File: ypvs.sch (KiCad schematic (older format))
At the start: 17 parts, among them J1 Servo, J2 LM_2596 _Input, J3 HV_Cable, J4 Motorcycle Battery, U2 LM1117-3.3, U3 H11L1

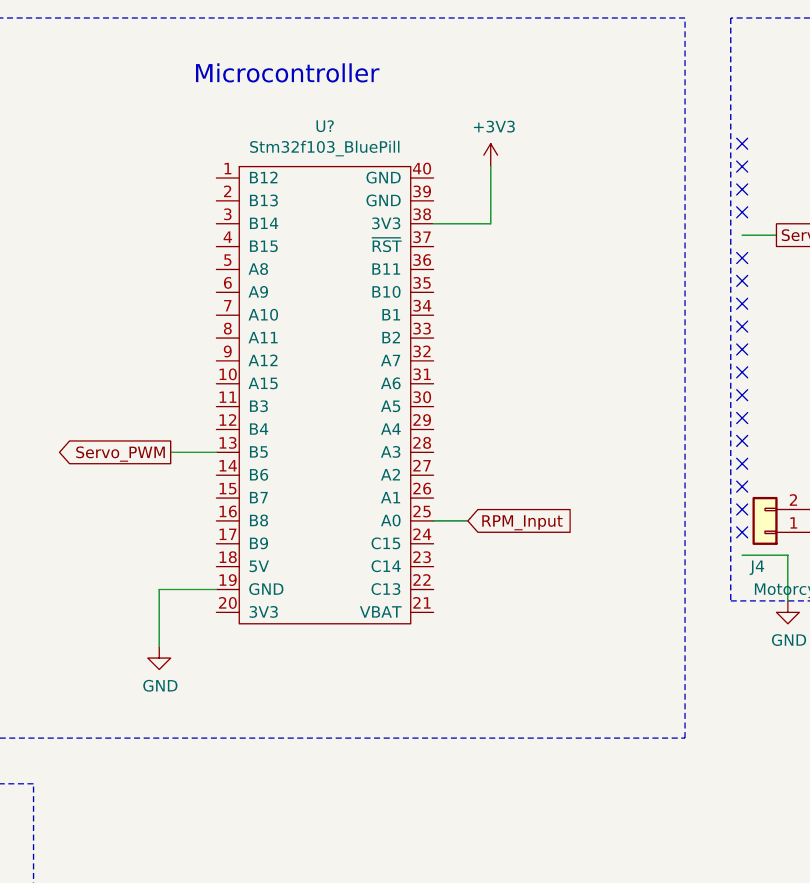
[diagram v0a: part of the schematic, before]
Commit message: added pcb outline and mounting holes
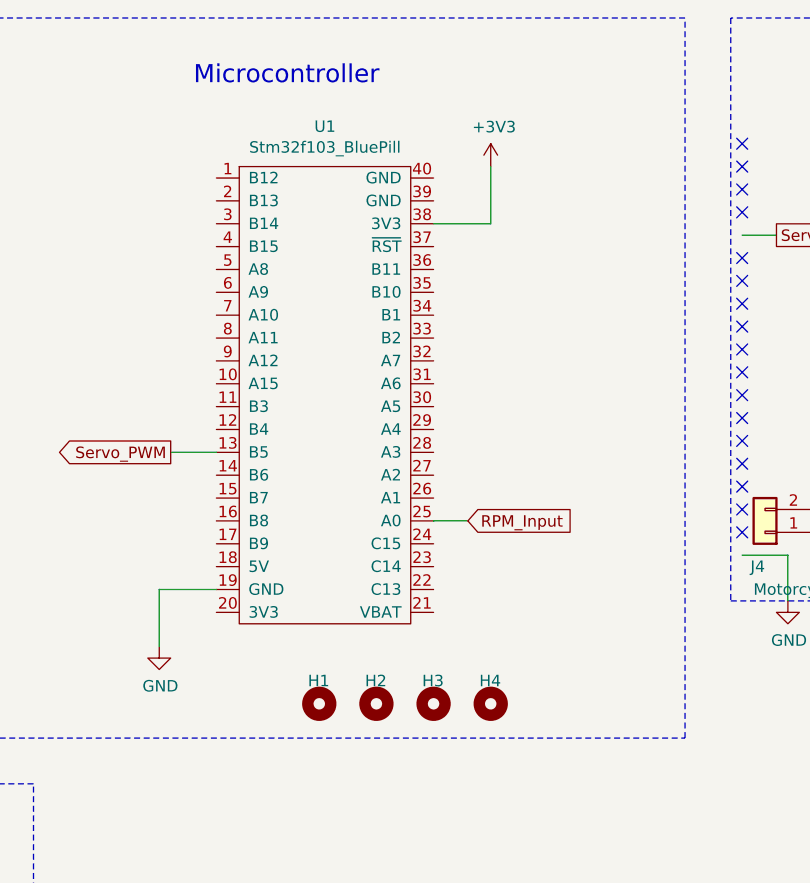
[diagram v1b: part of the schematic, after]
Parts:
- added H1, H2, H3, H4: MountingHole, MountingHole:MountingHole_2.7mm_M2.5, symbol Mechanical:MountingHole
- U1: renamed from U?; footprint (none) -> Package_DIP:DIP-40_W15.24mm_LongPads
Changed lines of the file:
@@
 	1250 5500 1350 5500
 $Comp
-L Ypvs:Stm32f103_BluePill U?
+L Ypvs:Stm32f103_BluePill U1
 U 1 1 5F48EF1D
 P 6050 2250
-F 0 "U?" H 6025 3375 50  0000 C CNN
+F 0 "U1" H 6025 3375 50  0000 C CNN
 F 1 "Stm32f103_BluePill" H 6025 3284 50  0000 C CNN
-F 2 "" H 6000 2200 50  0001 C CNN
+F 2 "Package_DIP:DIP-40_W15.24mm_LongPads" H 6000 2200 50  0001 C CNN
 F 3 "" H 6000 2200 50  0001 C CNN
 	1    6050 2250
@@
 Servo_PWM
 $Comp
-L power:+3V3 #PWR?
+L power:+3V3 #PWR0101
 U 1 1 5F4A4007
 P 6750 1300
-F 0 "#PWR?" H 6750 1150 50  0001 C CNN
+F 0 "#PWR0101" H 6750 1150 50  0001 C CNN
 F 1 "+3V3" H 6765 1473 50  0000 C CNN
 F 2 "" H 6750 1300 50  0001 C CNN
@@
 $EndComp
 $Comp
-L power:GND #PWR?
+L power:GND #PWR0102
 U 1 1 5F4A5041
 P 5300 3400
-F 0 "#PWR?" H 5300 3150 50  0001 C CNN
+F 0 "#PWR0102" H 5300 3150 50  0001 C CNN
 F 1 "GND" H 5305 3227 50  0000 C CNN
 F 2 "" H 5300 3400 50  0001 C CNN
@@
 Wire Wire Line
 	5300 3150 5300 3400
+$Comp
+L Mechanical:MountingHole H1
+U 1 1 5F4C806F
+P 6000 3650
+F 0 "H1" H 5950 3750 50  0000 L CNN
+F 1 "MountingHole" H 6100 3650 50  0001 L CNN
+F 2 "MountingHole:MountingHole_2.7mm_M2.5" H 6000 3650 50  0001 C CNN
+F 3 "~" H 6000 3650 50  0001 C CNN
+	1    6000 3650
+	1    0    0    -1
+$EndComp
+$Comp
+L Mechanical:MountingHole H2
+U 1 1 5F4C9D1D
+P 6250 3650
+F 0 "H2" H 6200 3750 50  0000 L CNN
+F 1 "MountingHole" H 6350 3650 50  0001 L CNN
+F 2 "MountingHole:MountingHole_2.7mm_M2.5" H 6250 3650 50  0001 C CNN
+F 3 "~" H 6250 3650 50  0001 C CNN
+	1    6250 3650
+	1    0    0    -1
+$EndComp
+$Comp
+L Mechanical:MountingHole H3
+U 1 1 5F4CA910
+P 6500 3650
+F 0 "H3" H 6450 3750 50  0000 L CNN
+F 1 "MountingHole" H 6600 3650 50  0001 L CNN
+F 2 "MountingHole:MountingHole_2.7mm_M2.5" H 6500 3650 50  0001 C CNN
+F 3 "~" H 6500 3650 50  0001 C CNN
+	1    6500 3650
+	1    0    0    -1
+$EndComp
+$Comp
+L Mechanical:MountingHole H4
+U 1 1 5F4CAE78
+P 6750 3650
+F 0 "H4" H 6700 3750 50  0000 L CNN
+F 1 "MountingHole" H 6850 3605 50  0001 L CNN
+F 2 "MountingHole:MountingHole_2.7mm_M2.5" H 6750 3650 50  0001 C CNN
+F 3 "~" H 6750 3650 50  0001 C CNN
+	1    6750 3650
+	1    0    0    -1
+$EndComp
 $EndSCHEMATC

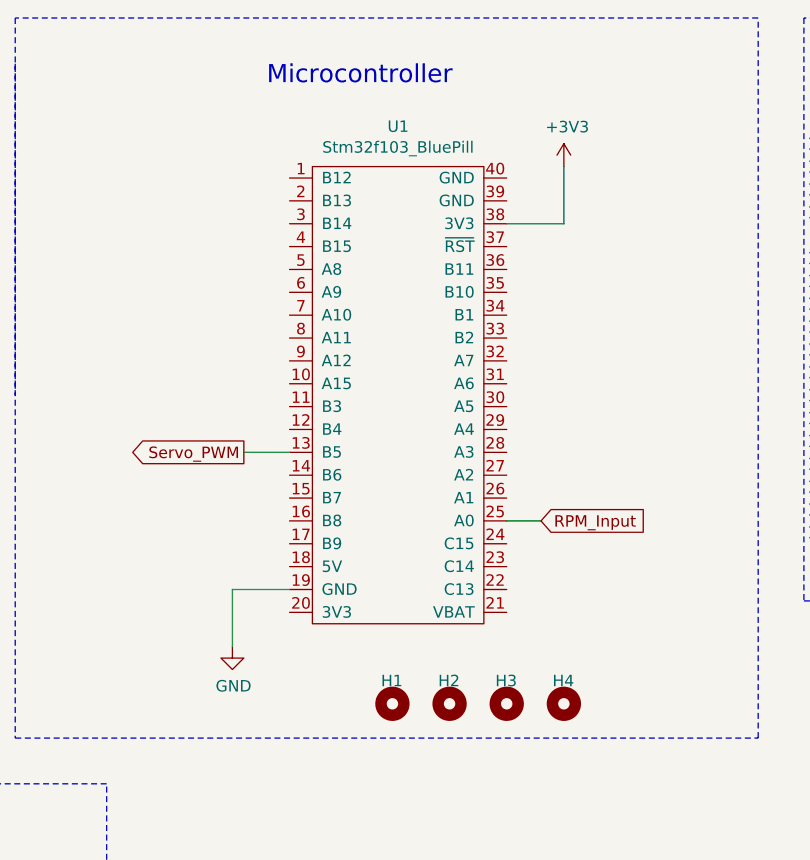
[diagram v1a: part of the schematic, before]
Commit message: Changed bluepill symbol
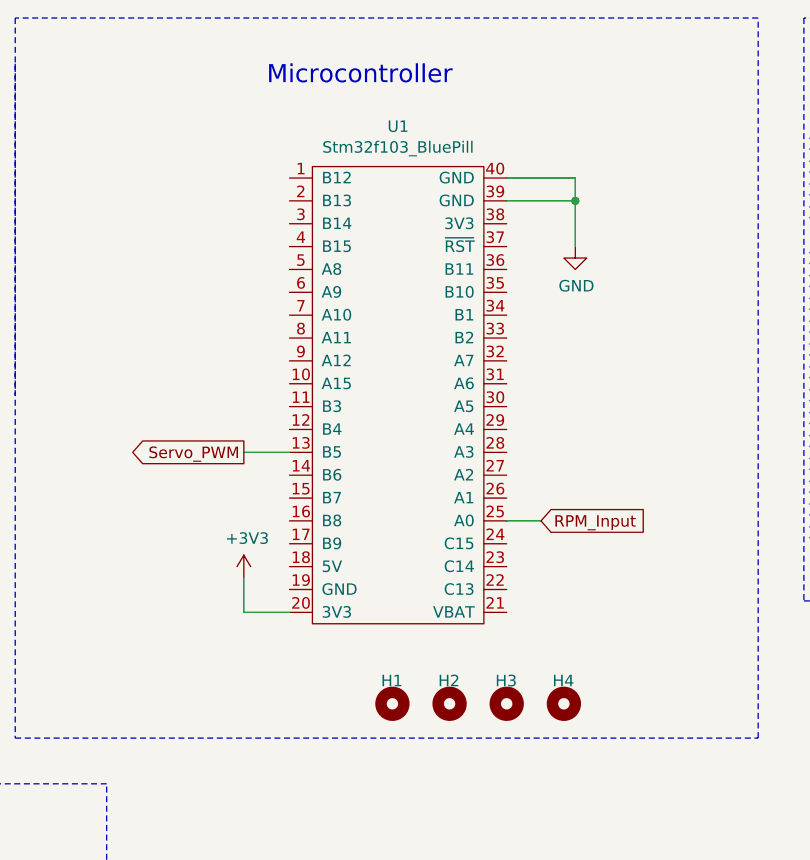
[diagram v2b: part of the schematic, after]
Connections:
- net +3V3: now also U1.20 (3V3); no longer U1.38 (3V3)
- net GND: now also U1.39 (GND), U1.40 (GND); no longer U1.19 (GND)
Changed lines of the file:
@@
 L power:+3V3 #PWR0101
 U 1 1 5F4A4007
-P 6750 1300
-F 0 "#PWR0101" H 6750 1150 50  0001 C CNN
-F 1 "+3V3" H 6765 1473 50  0000 C CNN
-F 2 "" H 6750 1300 50  0001 C CNN
-F 3 "" H 6750 1300 50  0001 C CNN
-	1    6750 1300
+P 5350 3100
+F 0 "#PWR0101" H 5350 2950 50  0001 C CNN
+F 1 "+3V3" H 5365 3273 50  0000 C CNN
+F 2 "" H 5350 3100 50  0001 C CNN
+F 3 "" H 5350 3100 50  0001 C CNN
+	1    5350 3100
 	1    0    0    -1
 $EndComp
@@
 L power:GND #PWR0102
 U 1 1 5F4A5041
-P 5300 3400
-F 0 "#PWR0102" H 5300 3150 50  0001 C CNN
-F 1 "GND" H 5305 3227 50  0000 C CNN
-F 2 "" H 5300 3400 50  0001 C CNN
-F 3 "" H 5300 3400 50  0001 C CNN
-	1    5300 3400
+P 6800 1650
+F 0 "#PWR0102" H 6800 1400 50  0001 C CNN
+F 1 "GND" H 6805 1477 50  0000 C CNN
+F 2 "" H 6800 1650 50  0001 C CNN
+F 3 "" H 6800 1650 50  0001 C CNN
+	1    6800 1650
 	1    0    0    -1
 $EndComp
@@
 Wire Wire Line
 	5550 2550 5350 2550
-Wire Wire Line
-	6500 1550 6750 1550
-Wire Wire Line
-	6750 1550 6750 1300
-Wire Wire Line
-	5550 3150 5300 3150
-Wire Wire Line
-	5300 3150 5300 3400
 $Comp
 L Mechanical:MountingHole H1
@@
 	1    0    0    -1
 $EndComp
+Wire Wire Line
+	5350 3100 5350 3250
+Wire Wire Line
+	5350 3250 5550 3250
+Wire Wire Line
+	6500 1450 6800 1450
+Wire Wire Line
+	6800 1450 6800 1650
+Wire Wire Line
+	6500 1350 6800 1350
+Wire Wire Line
+	6800 1350 6800 1450
+Connection ~ 6800 1450
 $EndSCHEMATC
